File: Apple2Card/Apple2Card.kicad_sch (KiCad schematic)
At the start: 59 parts, among them J1 ICSP, J2 Conn_01x25, J3 Conn_01x25, J4 Conn_01x16, J5 SERCON, J6 WIZNET 5500, SW1 SW_Push, U1 ATmega328P-P, U3 74HCT00, U4 82C55A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

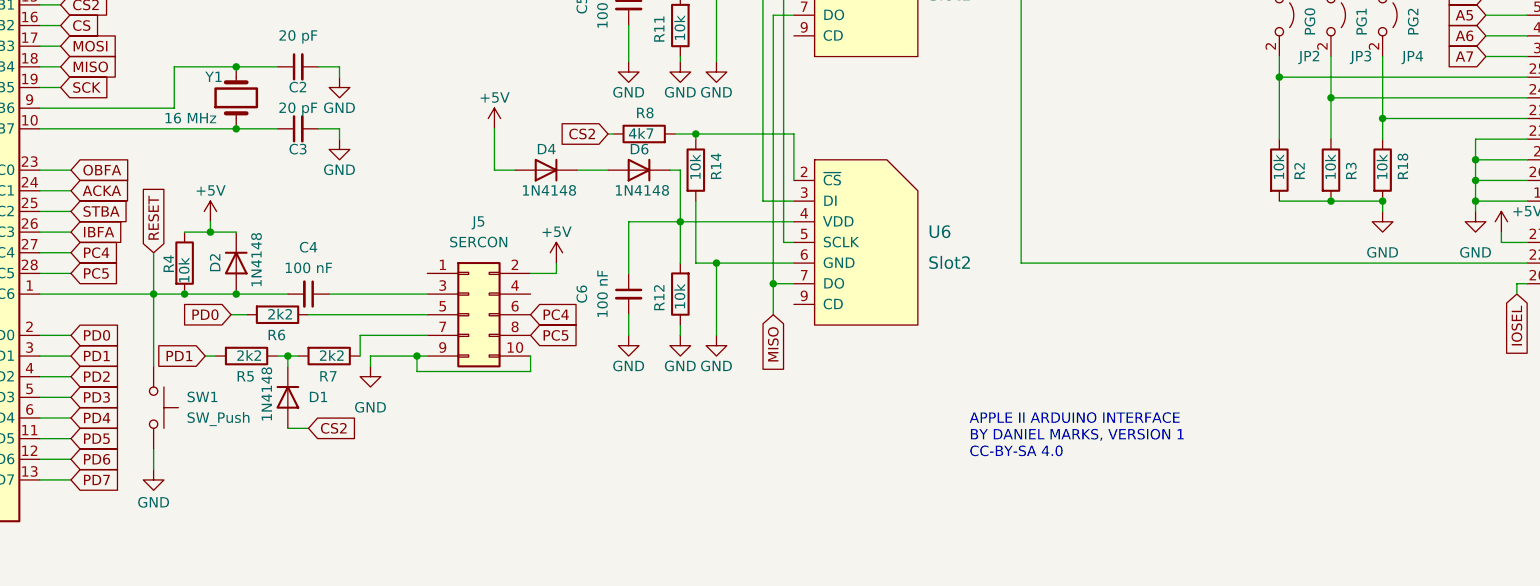
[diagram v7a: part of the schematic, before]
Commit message: Both slots working with real hardwarE
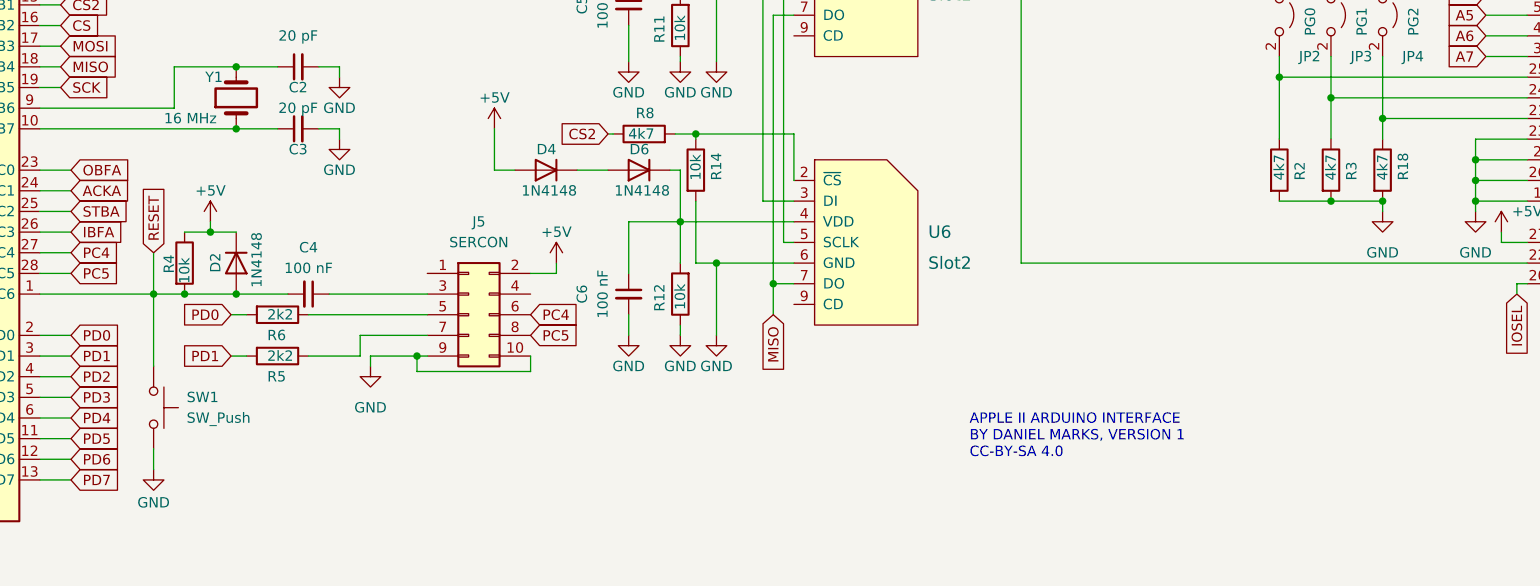
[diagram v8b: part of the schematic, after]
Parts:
- removed D1: 1N4148, Diode_THT:D_DO-35_SOD27_P7.62mm_Horizontal, symbol Device:D
- removed R7: 2k2, Resistor_THT:R_Axial_DIN0207_L6.3mm_D2.5mm_P7.62mm_Horizontal, symbol Device:R
- R18, R2, R3: value 10k -> 4k7
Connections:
- net at R5.1: now also J5.7 (Pin_7)
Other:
- moved on the sheet: R5
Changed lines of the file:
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@@
   (junction (at 46.99 86.36) (diameter 0) (color 0 0 0 0)
   )
-  (junction (at 101.6 163.83) (diameter 0) (color 0 0 0 0)
-  )
   (junction (at 55.88 100.33) (diameter 0) (color 0 0 0 0)
   )
@@
     (stroke (width 0) (type default) (color 0 0 0 0))
   )
-  (wire (pts (xy 100.33 163.83) (xy 101.6 163.83))
+  (wire (pts (xy 104.14 163.83) (xy 110.49 163.83))
     (stroke (width 0) (type default) (color 0 0 0 0))
   )
@@
     (stroke (width 0) (type default) (color 0 0 0 0))
   )
-  (wire (pts (xy 101.6 165.1) (xy 101.6 163.83))
-    (stroke (width 0) (type default) (color 0 0 0 0))
-  )
   (wire (pts (xy 229.87 110.49) (xy 229.87 116.84))
     (stroke (width 0) (type default) (color 0 0 0 0))
@@
     (stroke (width 0) (type default) (color 0 0 0 0))
   )
-  (wire (pts (xy 101.6 163.83) (xy 102.87 163.83))
-    (stroke (width 0) (type default) (color 0 0 0 0))
-  )
   (wire (pts (xy 236.22 73.66) (xy 238.76 73.66))
     (stroke (width 0) (type default) (color 0 0 0 0))
@@
     (stroke (width 0) (type default) (color 0 0 0 0))
   )
-  (wire (pts (xy 91.44 163.83) (xy 92.71 163.83))
+  (wire (pts (xy 94.615 163.83) (xy 96.52 163.83))
     (stroke (width 0) (type default) (color 0 0 0 0))
   )
@@
     (stroke (width 0) (type default) (color 0 0 0 0))
   )
-  (wire (pts (xy 101.6 172.72) (xy 104.14 172.72))
-    (stroke (width 0) (type default) (color 0 0 0 0))
-  )
   (wire (pts (xy 274.32 121.92) (xy 276.86 121.92))
     (stroke (width 0) (type default) (color 0 0 0 0))
@@
     )
   )
-  (global_label "PD1" (shape input) (at 91.44 163.83 180) (fields_autoplaced)
+  (global_label "PD1" (shape input) (at 94.615 163.83 180) (fields_autoplaced)
     (effects (font (size 1.27 1.27)) (justify right))
-    (property "Intersheet References" "${INTERSHEET_REFS}" (id 0) (at 85.3663 163.9094 0)
+    (property "Intersheet References" "${INTERSHEET_REFS}" (id 0) (at 88.5413 163.9094 0)
       (effects (font (size 1.27 1.27)) (justify right) hide)
     )
@@
     )
   )
-  (global_label "CS2" (shape input) (at 104.14 172.72 0) (fields_autoplaced)
-    (effects (font (size 1.27 1.27)) (justify left))
-    (property "Intersheet References" "${INTERSHEET_REFS}" (id 0) (at 110.1532 172.6406 0)
-      (effects (font (size 1.27 1.27)) (justify left) hide)
-    )
-  )
   (global_label "RW" (shape input) (at 34.29 71.12 0) (fields_autoplaced)
     (effects (font (size 1.27 1.27)) (justify left))
@@
     (pin "2")
   )
-  (symbol (lib_id "Device:D") (at 101.6 168.91 270) (unit 1)
-    (in_bom yes) (on_board yes)
-    (property "Reference" "D1" (id 0) (at 104.14 168.91 90)
-      (effects (font (size 1.27 1.27)) (justify left))
-    )
-    (property "Value" "1N4148" (id 1) (at 99.06 165.1 0)
-      (effects (font (size 1.27 1.27)) (justify left))
-    )
-    (property "Footprint" "Diode_THT:D_DO-35_SOD27_P7.62mm_Horizontal" (id 2) (at 101.6 168.91 0)
-      (effects (font (size 1.27 1.27)) hide)
-    )
-    (property "Datasheet" "~" (id 3) (at 101.6 168.91 0)
-      (effects (font (size 1.27 1.27)) hide)
-    )
-    (pin "1")
-    (pin "2")
-  )
   (symbol (lib_id "74xx:74HC00") (at 153.67 78.105 0) (unit 2)
     (in_bom yes) (on_board yes)
@@
     (pin "1")
   )
-  (symbol (lib_id "Device:R") (at 96.52 163.83 270) (unit 1)
+  (symbol (lib_id "Device:R") (at 100.33 163.83 270) (unit 1)
     (in_bom yes) (on_board yes)
-    (property "Reference" "R5" (id 0) (at 95.25 166.37 90)
+    (property "Reference" "R5" (id 0) (at 99.06 166.37 90)
       (effects (font (size 1.27 1.27)) (justify left))
     )
-    (property "Value" "2k2" (id 1) (at 95.25 163.83 90)
+    (property "Value" "2k2" (id 1) (at 99.06 163.83 90)
       (effects (font (size 1.27 1.27)) (justify left))
     )
-    (property "Footprint" "Resistor_THT:R_Axial_DIN0207_L6.3mm_D2.5mm_P7.62mm_Horizontal" (id 2) (at 96.52 162.052 90)
+    (property "Footprint" "Resistor_THT:R_Axial_DIN0207_L6.3mm_D2.5mm_P7.62mm_Horizontal" (id 2) (at 100.33 162.052 90)
       (effects (font (size 1.27 1.27)) hide)
     )
-    (property "Datasheet" "~" (id 3) (at 96.52 163.83 0)
+    (property "Datasheet" "~" (id 3) (at 100.33 163.83 0)
       (effects (font (size 1.27 1.27)) hide)
     )
@@
       (effects (font (size 1.27 1.27)) (justify left))
     )
-    (property "Value" "10k" (id 1) (at 229.87 142.24 90)
+    (property "Value" "4k7" (id 1) (at 229.87 142.24 90)
       (effects (font (size 1.27 1.27)) (justify left))
     )
@@
       (effects (font (size 1.27 1.27)) (justify left))
     )
-    (property "Value" "10k" (id 1) (at 236.22 142.24 90)
+    (property "Value" "4k7" (id 1) (at 236.22 142.24 90)
       (effects (font (size 1.27 1.27)) (justify left))
     )
@@
       (effects (font (size 1.27 1.27)) (justify left))
     )
-    (property "Value" "10k" (id 1) (at 223.52 142.24 90)
+    (property "Value" "4k7" (id 1) (at 223.52 142.24 90)
       (effects (font (size 1.27 1.27)) (justify left))
     )
@@
     (pin "1")
   )
-  (symbol (lib_id "Device:R") (at 106.68 163.83 270) (unit 1)
-    (in_bom yes) (on_board yes)
-    (property "Reference" "R7" (id 0) (at 105.41 166.37 90)
-      (effects (font (size 1.27 1.27)) (justify left))
-    )
-    (property "Value" "2k2" (id 1) (at 105.41 163.83 90)
-      (effects (font (size 1.27 1.27)) (justify left))
-    )
-    (property "Footprint" "Resistor_THT:R_Axial_DIN0207_L6.3mm_D2.5mm_P7.62mm_Horizontal" (id 2) (at 106.68 162.052 90)
-      (effects (font (size 1.27 1.27)) hide)
-    )
-    (property "Datasheet" "~" (id 3) (at 106.68 163.83 0)
-      (effects (font (size 1.27 1.27)) hide)
-    )
-    (pin "1")
-    (pin "2")
-  )
   (symbol (lib_id "power:GND") (at 257.81 92.71 0) (unit 1)
     (in_bom yes) (on_board yes) (fields_autoplaced)
@@
       (reference "C14") (unit 1) (value "10 uF") (footprint "Capacitor_THT:CP_Radial_D5.0mm_P2.50mm")
     )
-    (path "/1a56e58d-4861-4368-bc46-6f7f32ce30f2"
-      (reference "D1") (unit 1) (value "1N4148") (footprint "Diode_THT:D_DO-35_SOD27_P7.62mm_Horizontal")
-    )
     (path "/7f3fa796-9760-4b6f-8396-ff154fbd25d2"
       (reference "D2") (unit 1) (value "1N4148") (footprint "Diode_THT:D_DO-35_SOD27_P7.62mm_Horizontal")
@@
     )
     (path "/9d68934e-289f-4086-8681-226d8e8ece6c"
-      (reference "R2") (unit 1) (value "10k") (footprint "Resistor_THT:R_Axial_DIN0207_L6.3mm_D2.5mm_P7.62mm_Horizontal")
+      (reference "R2") (unit 1) (value "4k7") (footprint "Resistor_THT:R_Axial_DIN0207_L6.3mm_D2.5mm_P7.62mm_Horizontal")
     )
     (path "/30cf679f-f876-483a-95b7-40e075914504"
-      (reference "R3") (unit 1) (value "10k") (footprint "Resistor_THT:R_Axial_DIN0207_L6.3mm_D2.5mm_P7.62mm_Horizontal")
+      (reference "R3") (unit 1) (value "4k7") (footprint "Resistor_THT:R_Axial_DIN0207_L6.3mm_D2.5mm_P7.62mm_Horizontal")
     )
     (path "/a0cd4d38-f115-45f2-83be-7b9c48e4716b"
@@
       (reference "R6") (unit 1) (value "2k2") (footprint "Resistor_THT:R_Axial_DIN0207_L6.3mm_D2.5mm_P7.62mm_Horizontal")
     )
-    (path "/d37a4804-d762-400d-853b-69c4aa54bb24"
-      (reference "R7") (unit 1) (value "2k2") (footprint "Resistor_THT:R_Axial_DIN0207_L6.3mm_D2.5mm_P7.62mm_Horizontal")
-    )
     (path "/52e3953b-4d68-4321-8211-9cf39a764231"
       (reference "R8") (unit 1) (value "4k7") (footprint "Resistor_THT:R_Axial_DIN0207_L6.3mm_D2.5mm_P7.62mm_Horizontal")
@@
     )
     (path "/851fb17c-7aa0-4a55-bd2b-57d525ad389f"
-      (reference "R18") (unit 1) (value "10k") (footprint "Resistor_THT:R_Axial_DIN0207_L6.3mm_D2.5mm_P7.62mm_Horizontal")
+      (reference "R18") (unit 1) (value "4k7") (footprint "Resistor_THT:R_Axial_DIN0207_L6.3mm_D2.5mm_P7.62mm_Horizontal")
     )
     (path "/e79fc384-74dc-484b-a360-270761f9e177"
